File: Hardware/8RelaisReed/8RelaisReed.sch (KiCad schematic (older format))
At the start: 28 parts, among them J1 ISP, P1 5VIN, P10 CONN_01X02, P11 CONN_01X02, P4 CONN_01X02, P5 CONN_01X02, P6 CONN_01X02, P7 CONN_01X02, P8 CONN_01X02, P9 CONN_01X02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

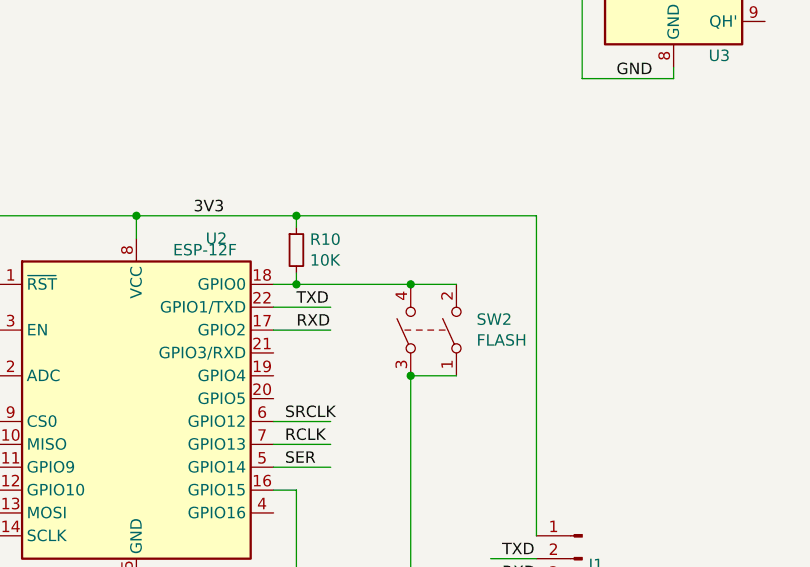
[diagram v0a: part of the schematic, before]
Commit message: - Modified almost all hardware boards : They were missing a pull-up resistor on GPIO2, which made impossible to flash. - Updated baseBoard.* files
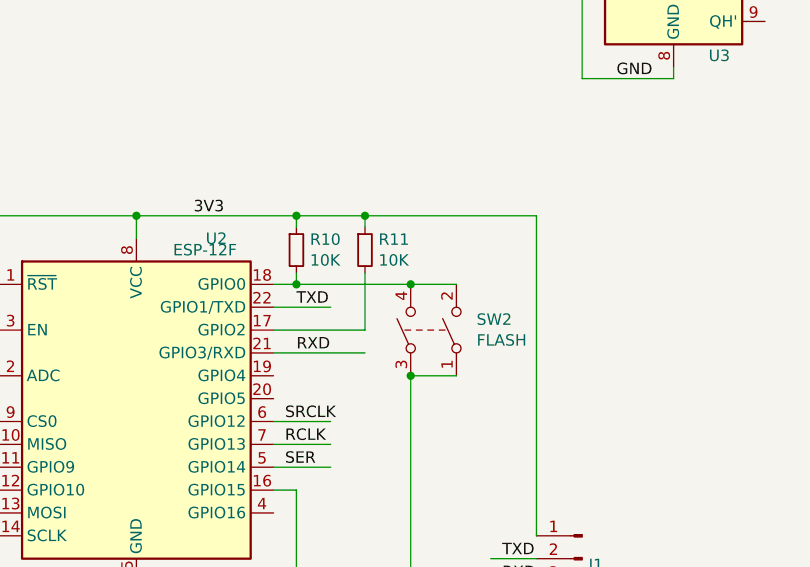
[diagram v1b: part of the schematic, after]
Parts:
- added R11: 10K, Resistor_SMD:R_0805_2012Metric_Pad1.15x1.40mm_HandSolder, symbol Device:R_Small
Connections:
- wire segments 121 -> 125
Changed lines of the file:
@@
 	3900 4200 3900 2800
 Wire Wire Line
-	3900 2800 2850 2800
+	3900 2800 3150 2800
 Connection ~ 2850 2800
 Wire Wire Line
@@
 Wire Wire Line
 	3000 3200 2750 3200
-Wire Wire Line
-	3000 3300 2750 3300
 Text Label 2850 3200 0    50   ~ 0
 TXD
-Text Label 2850 3300 0    50   ~ 0
+Text Label 2850 3400 0    50   ~ 0
 RXD
 Text Label 3750 4300 0    50   ~ 0
@@
 Text Label 3750 4400 0    50   ~ 0
 RXD
+$Comp
+L Device:R_Small R11
+U 1 1 5C80A805
+P 3150 2950
+F 0 "R11" H 3209 2996 50  0000 L CNN
+F 1 "10K" H 3209 2905 50  0000 L CNN
+F 2 "Resistor_SMD:R_0805_2012Metric_Pad1.15x1.40mm_HandSolder" H 3150 2950 50  0001 C CNN
+F 3 "~" H 3150 2950 50  0001 C CNN
+	1    3150 2950
+	1    0    0    -1
+$EndComp
+Wire Wire Line
+	3150 2850 3150 2800
+Connection ~ 3150 2800
+Wire Wire Line
+	3150 2800 2850 2800
+Wire Wire Line
+	2750 3300 3150 3300
+Wire Wire Line
+	3150 3300 3150 3050
+Wire Wire Line
+	2750 3400 3150 3400
 $EndSCHEMATC

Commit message: Fix on the BaseBoard class
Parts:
- removed C1, C2: 10uF, Capacitor_SMD:C_0805_2012Metric_Pad1.15x1.40mm_HandSolder, symbol 8RelaisReed-rescue:C-mySensors_8RelaisReed-rescue
- removed J1: ISP, Connector_PinHeader_2.54mm:PinHeader_1x04_P2.54mm_Vertical, symbol Connector:Conn_01x04_Male
- removed P1: 5VIN, Connectors:bornier2, symbol 8RelaisReed-rescue:CONN_01X02-mySensors_8RelaisReed-rescue
- removed R10, R11, R9: 10K, Resistor_SMD:R_0805_2012Metric_Pad1.15x1.40mm_HandSolder, symbol Device:R_Small
- removed SW1: SW_DPST, Button_Switch_SMD:SW_SPST_EVPBF, symbol Switch:SW_DPST
- removed SW2: FLASH, Button_Switch_SMD:SW_SPST_EVPBF, symbol Switch:SW_DPST
- removed U1: AMS1117, TO_SOT_Packages_SMD:SOT-223, symbol 8RelaisReed-rescue:AMS1117-mySensors_8RelaisReed-rescue
- removed U2: ESP-12F, RF_Module:ESP-12E, symbol RF_Module:ESP-12F
- added J1: Conn_02x03_Odd_Even, Connector_PinHeader_2.54mm:PinHeader_2x03_P2.54mm_Vertical, symbol Connector_Generic:Conn_02x03_Odd_Even
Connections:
- net labels removed: RXD, TXD
- wire segments 125 -> 76
